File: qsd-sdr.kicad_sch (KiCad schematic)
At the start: 55 parts, among them J11 SDR ANT, J12 SDR Out, U5 OPA1612AxD, U7 SN74CBT3253, U8 OPA1612AxD

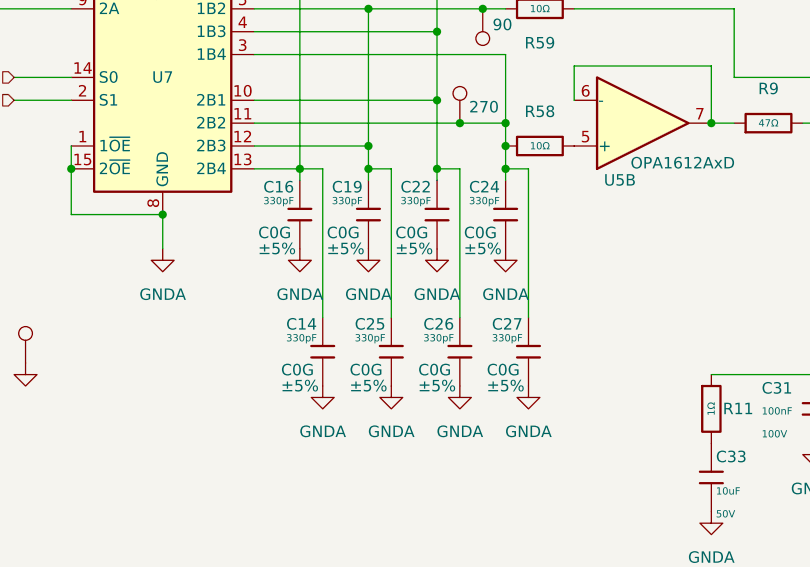
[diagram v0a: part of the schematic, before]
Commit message: Changed C_sample to 10nf
And added 10 Ohm damping resistors.
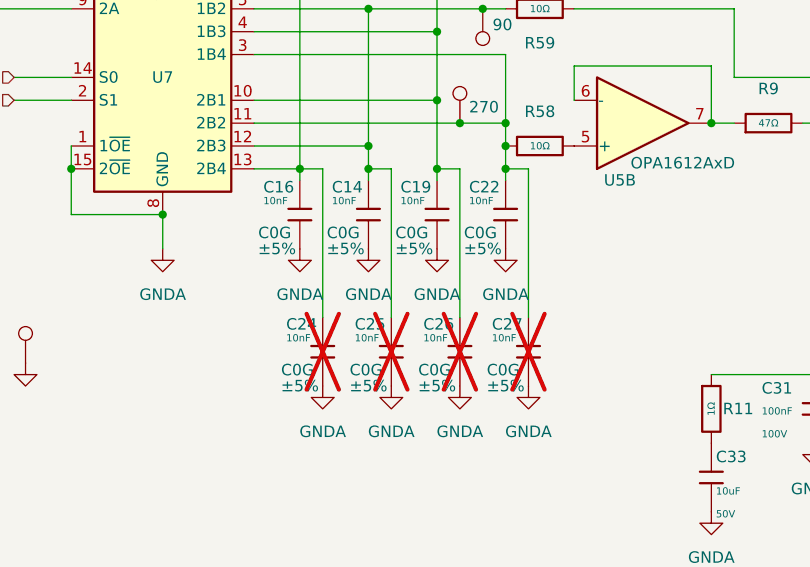
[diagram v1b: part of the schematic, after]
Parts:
- C14, C16, C19, C22: value 330pF -> 10nF; Attrition Qty 10 -> (none); Capacitance 330pF -> 10nF; Category Capacitors,Multilayer Ceramic Capacitors MLCC - SMD/SMT -> C0CG; Manufacturer Samsung Electro-Mechanics -> (none); Minimum Qty 20 -> 1; Part CL10C331JB8NNNC -> (none)
- C24, C25, C26, C27: value 330pF -> 10nF; Attrition Qty 10 -> (none); Capacitance 330pF -> 10nF; Category Capacitors,Multilayer Ceramic Capacitors MLCC - SMD/SMT -> C0CG; Manufacturer Samsung Electro-Mechanics -> (none); Minimum Qty 20 -> 1; Part CL10C331JB8NNNC -> (none); now not fitted
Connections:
- net at C16.1, R60.1, TP14.1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: now also C24.1; no longer C14.1
- net at C26.1, R61.1, TP6.1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: now also C19.1; no longer C22.1
- net at C25.1, R59.1, TP16.1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: now also C14.1; no longer C19.1
- net at C27.1, R58.1, TP7.1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: now also C22.1; no longer C24.1

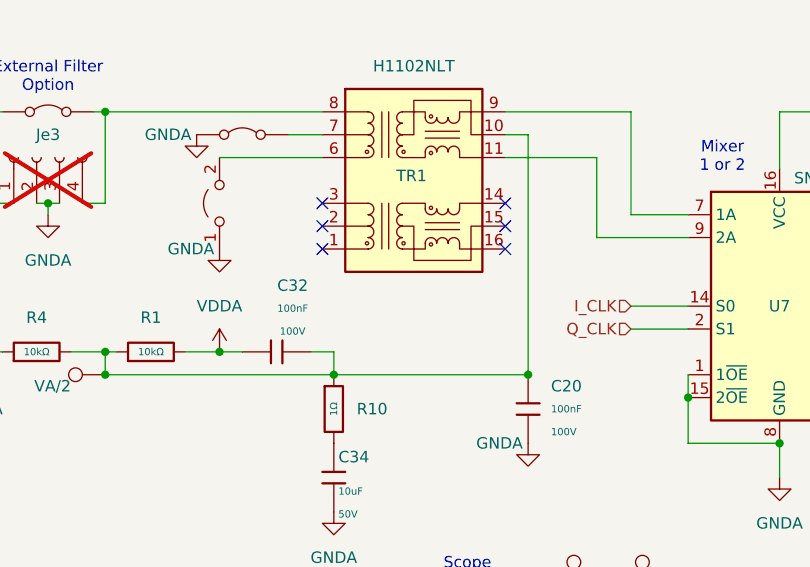
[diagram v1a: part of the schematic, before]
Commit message: Changed R55-58 values.
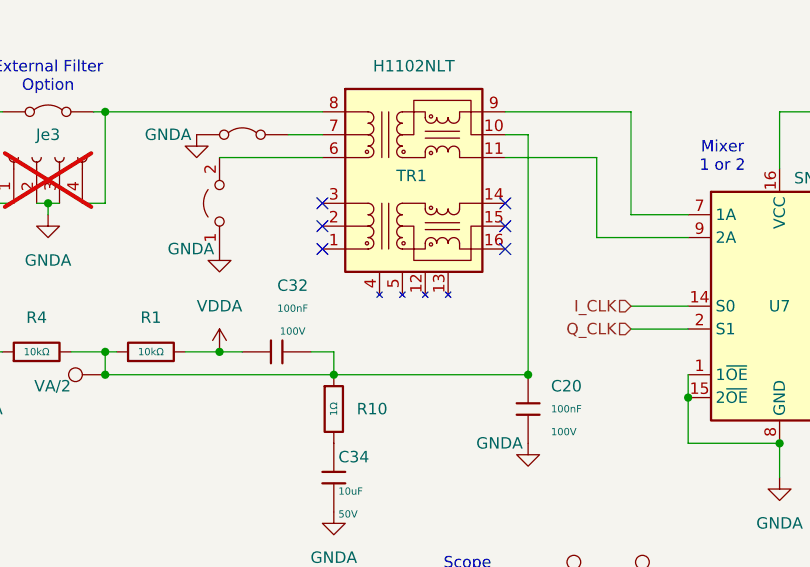
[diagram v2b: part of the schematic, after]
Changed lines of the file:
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@@
 		(pin "9"
+		)
+		(pin "5"
+		)
+		(pin "13"
+		)
+		(pin "12"
+		)
+		(pin "4"
 		)
 		(instances

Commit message: Moved DAC jack and planes.
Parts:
- C24, C25, C26, C27: now fitted
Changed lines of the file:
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@@
 		(in_bom yes)
 		(on_board yes)
-		(dnp yes)
+		(dnp no)
 		(property "Reference" "C27"
 			(at 167.386 121.412 0)
@@
 		(in_bom yes)
 		(on_board yes)
-		(dnp yes)
+		(dnp no)
+		(fields_autoplaced yes)
 		(property "Reference" "C24"
-			(at 144.526 121.412 0)
+			(at 146.05 120.6499 0)
 			(effects
 				(font
 					(size 1.27 1.27)
 				)
-				(justify left)
+				(justify right)
 			)
 		)
 		(property "Value" "10nF"
-			(at 144.526 122.936 0)
+			(at 146.05 123.19 0)
 			(effects
 				(font
 					(size 0.8 0.8)
 				)
-				(justify left)
+				(justify right)
 			)
 		)
@@
 		)
 		(property "Tolerance" "±5%"
-			(at 146.05 128.27 0)
+			(at 146.05 125.7299 0)
 			(effects
 				(font
 					(size 1.27 1.27)
 				)
+				(justify right)
 			)
 		)
@@
 		)
 		(property "Temperature Coefficient" "C0G"
-			(at 145.796 126.492 0)
+			(at 146.05 128.2699 0)
 			(effects
 				(font
 					(size 1.27 1.27)
 				)
+				(justify right)
 			)
 		)
@@
 		(in_bom yes)
 		(on_board yes)
-		(dnp yes)
+		(dnp no)
 		(property "Reference" "C26"
 			(at 159.766 121.412 0)
@@
 		(in_bom yes)
 		(on_board yes)
-		(dnp yes)
+		(dnp no)
 		(property "Reference" "C25"
 			(at 152.146 121.412 0)

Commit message: No Errors No Warnings
Some were excluded.
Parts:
- removed C24, C25, C26, C27: 10nF, PCM_JLCPCB:C_0603, symbol PCM_JLCPCB-Capacitors:0603,330pF

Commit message: Fixed U7 to the right part (C2674552)
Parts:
- U7: LCSC C2674583 -> C2674552
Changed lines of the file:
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@@
 			)
 		)
-		(property "LCSC" "C2674583"
+		(property "LCSC" "C2674552"
 			(at 130.81 93.98 0)
 			(effects
